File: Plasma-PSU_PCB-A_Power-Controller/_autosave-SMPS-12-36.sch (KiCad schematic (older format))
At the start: 10 parts, among them J301 Arduino_Pinout_01-15, J302 SPI, J303 UART, J304 I2C, J305 Arduino_Pinout_16-30

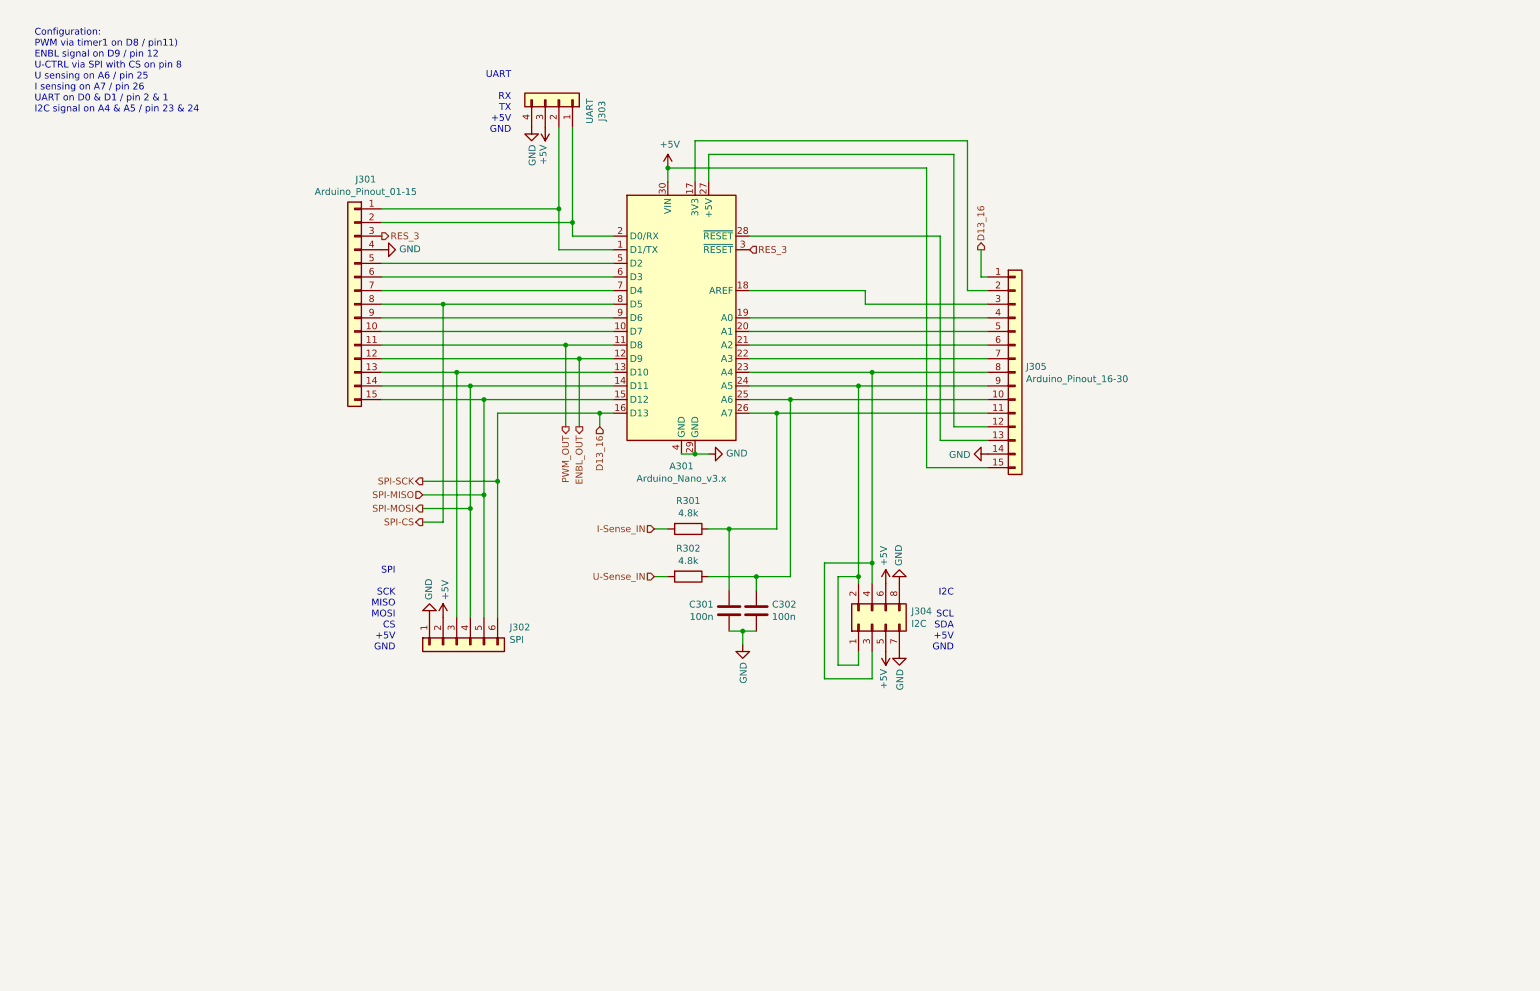
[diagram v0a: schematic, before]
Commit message: BOM PCB-B arranged
Order numbers for Farnell-element14 and for Mouser
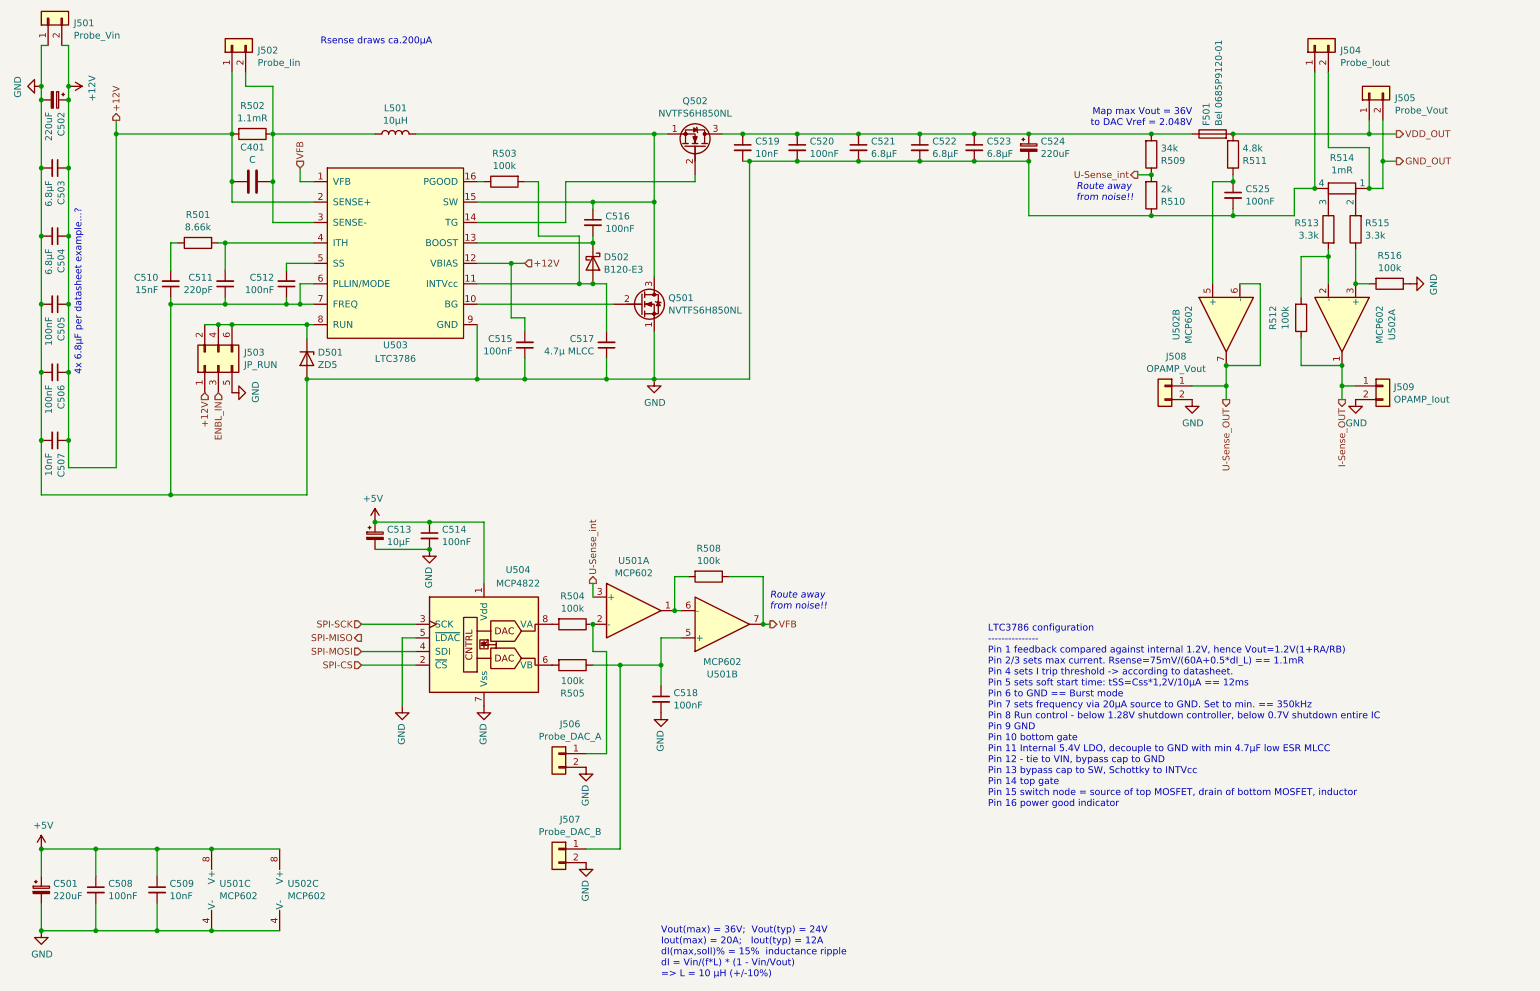
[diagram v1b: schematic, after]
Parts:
- removed A301: Arduino_Nano_v3.x, Module:Arduino_Nano, symbol MCU_Module:Arduino_Nano_v3.x
- removed C301, C302: 100n, Capacitor_SMD:C_0201_0603Metric, symbol Device:C
- removed J301: Arduino_Pinout_01-15, Connector_PinHeader_2.54mm:PinHeader_1x15_P2.54mm_Vertical, symbol Connector_Generic:Conn_01x15
- removed J302: SPI, Connector_PinHeader_2.54mm:PinHeader_1x06_P2.54mm_Vertical, symbol Connector_Generic:Conn_01x06
- removed J303: UART, Connector_PinHeader_2.54mm:PinHeader_1x04_P2.54mm_Vertical, symbol Connector_Generic:Conn_01x04
- removed J304: I2C, Connector_PinHeader_2.54mm:PinHeader_2x04_P2.54mm_Vertical, symbol Connector_Generic:Conn_02x04_Odd_Even
- removed J305: Arduino_Pinout_16-30, Connector_PinHeader_2.54mm:PinHeader_1x15_P2.54mm_Vertical, symbol Connector_Generic:Conn_01x15
- removed R301, R302: 4.8k, Resistor_THT:R_Axial_DIN0207_L6.3mm_D2.5mm_P7.62mm_Horizontal, symbol Device:R
- added C401: C, symbol Device:C
- added C501, C502, C524: 220uF, Capacitor_THT:CP_Radial_D8.0mm_P3.50mm, symbol Device:CP_Small
- added C503, C504, C521, C522, C523: 6.8µF, Capacitor_SMD:C_1206_3216Metric, symbol Device:C_Small
- added C505, C506, C508, C512, C514, C515, C516, C518, C520, C525: 100nF, Capacitor_SMD:C_1206_3216Metric, symbol Device:C_Small
- added C507, C509, C519: 10nF, Capacitor_SMD:C_0805_2012Metric, symbol Device:C_Small
- added C510: 15nF, Capacitor_SMD:C_0805_2012Metric, symbol Device:C_Small
- added C511: 220pF, Capacitor_SMD:C_0805_2012Metric, symbol Device:C_Small
- added C513: 10µF, Capacitor_SMD:C_Elec_6.3x5.8, symbol Device:CP_Small
- added C517: 4.7µ MLCC, Capacitor_SMD:C_1206_3216Metric, symbol Device:C_Small
- added D501: ZD5, Diode_SMD:D_SOD-323, symbol Device:D_Zener
- added D502: B120-E3, Diode_SMD:D_SMA, symbol Diode:B120-E3
- added F501: Bel 0685P9120-01, Fuse:Fuse_1206_3216Metric_Pad1.42x1.75mm_HandSolder, symbol Device:Fuse
- added J501: Probe_Vin, TestPoint:TestPoint_2Pads_Pitch5.08mm_Drill1.3mm, symbol Connector_Generic:Conn_01x02
- added J502: Probe_Iin, TestPoint:TestPoint_2Pads_Pitch5.08mm_Drill1.3mm, symbol Connector_Generic:Conn_01x02
- added J503: JP_RUN, Connector_PinHeader_2.54mm:PinHeader_2x03_P2.54mm_Vertical, symbol Connector_Generic:Conn_02x03_Odd_Even
- added J504: Probe_Iout, TestPoint:TestPoint_2Pads_Pitch5.08mm_Drill1.3mm, symbol Connector_Generic:Conn_01x02
- added J505: Probe_Vout, TestPoint:TestPoint_2Pads_Pitch5.08mm_Drill1.3mm, symbol Connector_Generic:Conn_01x02
- added J506: Probe_DAC_A, TestPoint:TestPoint_2Pads_Pitch5.08mm_Drill1.3mm, symbol Connector_Generic:Conn_01x02
- added J507: Probe_DAC_B, TestPoint:TestPoint_2Pads_Pitch5.08mm_Drill1.3mm, symbol Connector_Generic:Conn_01x02
- added J508: OPAMP_Vout, TestPoint:TestPoint_2Pads_Pitch5.08mm_Drill1.3mm, symbol Connector_Generic:Conn_01x02
- added J509: OPAMP_Iout, TestPoint:TestPoint_2Pads_Pitch5.08mm_Drill1.3mm, symbol Connector_Generic:Conn_01x02
- added L501: 10µH, symbol Device:L
- added Q501, Q502: NVTFS6H850NL, Plasma-PSU_PCB-A_Power-Controller:ONSEMI-µ8FL, symbol Device:Q_NMOS_SGD
- added R501: 8.66k, Resistor_SMD:R_0805_2012Metric, symbol Device:R
- added R502: 1.1mR, Resistor_SMD:R_2512_6332Metric, symbol Device:R
- added R503, R504, R505, R508, R512, R516: 100k, Resistor_SMD:R_0805_2012Metric, symbol Device:R
- added R509: 34k, Resistor_SMD:R_0805_2012Metric, symbol Device:R
- added R510: 2k, Resistor_SMD:R_0805_2012Metric, symbol Device:R
- added R511: 4.8k, Resistor_SMD:R_0805_2012Metric, symbol Device:R
- added R513, R515: 3.3k, Resistor_SMD:R_0805_2012Metric, symbol Device:R
- added R514: 1mR, Resistor_SMD:R_2512_6332Metric, symbol Device:R_Shunt
- added U501, U502: MCP602, Package_SO:SOIC-8_3.9x4.9mm_P1.27mm, symbol Amplifier_Operational:MCP602
- added U503: LTC3786, Package_DFN_QFN:QFN-16-1EP_3x3mm_P0.5mm_EP1.45x1.45mm_ThermalVias, symbol Regulator_Switching:LTC3786
- added U504: MCP4822, Package_SO:SOIC-8_3.9x4.9mm_P1.27mm, symbol Analog_DAC:MCP4822
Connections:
- net +5V: now also C501.1, C508.1, C509.1, C513.1, C514.1, U501.8 (V+), U502.8 (V+), U504.1 (Vdd)
- net GND: now also C501.2, C502.2, C503.2, C504.2, C505.2, C506.2, C507.2, C508.2, C509.2, C510.1, C511.1, C512.1, C513.2, C514.2, C515.1, C517.1, C518.2, C519.2, C520.2, C521.2, C522.2, C523.2, C524.2, C525.2, D501.2 (A), J501.1 (Pin_1), J503.5 (Pin_5), J504.1 (Pin_1), J506.2 (Pin_2), J507.2 (Pin_2), J508.2 (Pin_2), J509.2 (Pin_2), Q501.1 (S), R510.1, R514.4, R516.1, U501.4 (V-), U502.4 (V-), U503.6 (PLLIN/MODE), U503.7 (FREQ), U503.9 (GND), U504.5 (~LDAC), U504.7 (Vss)
- net SPI-CS: now also U504.2 (~CS)
- net SPI-MOSI: now also U504.4 (SDI)
- new net: C519.1, C520.1, C521.1, C522.1, C523.1, C524.1, F501.1, Q502.3 (D), R509.2
- new net: C525.1, R511.1, U502.5 (+)
- new net: R514.2, R515.2
- new net: R513.1, R514.3
- new net: R512.2, R513.2, U502.2 (-)
- new net: R515.1, R516.2, U502.3 (+)
- new net: C518.1, J507.1 (Pin_1), R505.1, U501.5 (+)
- new net: R508.2, U501.1, U501.6 (-)
- new net: Q501.2 (G), U503.10 (BG)
- new net: C516.1, L501.2, Q501.3 (D), Q502.1 (S), U503.15 (SW)
- new net: Q502.2 (G), U503.14 (TG)
- new net: C517.2, D502.2 (A), R503.2, U503.11 (INTVcc)
- new net: C516.2, D502.1 (K), U503.13 (BOOST)
- new net: R503.1, U503.16 (PGOOD)
- new net: C401.2, J502.2 (Pin_2), L501.1, R502.1, U503.3 (SENSE-)
- new net: C511.2, R501.2, U503.4 (ITH)
- new net: C512.2, U503.5 (SS)
- new net: D501.1 (K), J503.2 (Pin_2), J503.4 (Pin_4), J503.6 (Pin_6), U503.8 (RUN)
- new net: R505.2, U504.6 (VB)
- new net: R504.2, U504.8 (VA)
- new net: J506.1 (Pin_1), R504.1, U501.2 (-)
- new net: C510.2, R501.1
- new net +12V: C401.1, C502.1, C503.1, C504.1, C505.1, C506.1, C507.1, C515.2, J501.2 (Pin_2), J502.1 (Pin_1), J503.1 (Pin_1), R502.2, U503.12 (VBIAS), U503.2 (SENSE+)
- new net ENBL_IN: J503.3 (Pin_3)
- new net GND_OUT: J504.2 (Pin_2), J505.2 (Pin_2), R514.1
- new net I-Sense_OUT: J509.1 (Pin_1), R512.1, U502.1
- new net SPI-SCK: U504.3 (SCK)
- new net U-Sense_OUT: J508.1 (Pin_1), U502.6 (-), U502.7
- new net U-Sense_int: R509.1, R510.2, U501.3 (+)
- new net VDD_OUT: F501.2, J505.1 (Pin_1), R511.2
- new net VFB: R508.1, U501.7, U503.1 (VFB)
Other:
- note added: "4x 6.8µF per datasheet example...?"
- note added: "LTC3786 configuration\n---------------\nPin 1 feedback compared against internal 1.2V, hence Vout=1.2V(1+RA/RB)\nPin 2/3 sets max current. Rsense=75mV/(60A+0.5*dI_L) == 1.1mR \nPin 4 sets I trip threshold -> according to datasheet.\nPin 5 sets soft start time: tSS=Css*1,2V/10µA == 12ms\nPin 6 to GND == Burst mode\nPin 7 sets frequency via 20µA source to GND. Set to min. == 350kHz\nPin 8 Run contr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"
- note added: "Map max Vout = 36V \nto DAC Vref = 2.048V"
- note added: "Route away \nfrom noise!!"
- note added: "Rsense draws ca.200µA"
- note added: "Vout(max) = 36V; Vout(typ) = 24V\nIout(max) = 20A; Iout(typ) = 12A\ndI(max,soll)% = 15% inductance ripple\ndI = Vin/(f*L) * (1 - Vin/Vout)\n=> L = 10 µH (+/-10%)"
- note removed: "Configuration:\nPWM via timer1 on D8 / pin11)\nENBL signal on D9 / pin 12\nU-CTRL via SPI with CS on pin 8\nU sensing on A6 / pin 25\nI sensing on A7 / pin 26\nUART on D0 & D1 / pin 2 & 1\nI2C signal on A4 & A5 / pin 23 & 24"
- note removed: "I2C\n\nSCL\nSDA\n+5V\nGND"
- note removed: "SPI\n\nSCK\nMISO\nMOSI\nCS\n+5V\nGND"
- note removed: "UART\n\nRX\nTX\n+5V\nGND"
